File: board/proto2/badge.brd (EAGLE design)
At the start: 136.5 x 119 mm, 66 parts, among them IC1 TLV62569, J1 5051101092, J2 M05X2X1.27

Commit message: layout in process
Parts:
- added OLED1: CFAF128128B, badge:CFAF128128B
- moved C28 615.5 mm to (41.9, 92.2), turned to 305 degrees
- moved J2 590.4 mm to (43.1, 93.9), turned to 35 degrees
- moved C25 583.9 mm to (50.3, 68.8), turned to 90 degrees
- moved C24 582.9 mm to (43.2, 73.4)
- moved SD1 550.9 mm to (31.5, 69.6), turned to 35 degrees
- moved S7 548.5 mm to (90.8, 80.0), turned to 90 degrees
- moved C22 531.7 mm to (88.4, 64.9), turned to 68 degrees
- moved C20 526.9 mm to (87.9, 65.1), turned to 68 degrees
- moved C21 525.4 mm to (88.1, 65.0), turned to 68 degrees
- moved C18 519.3 mm to (88.4, 62.1), turned to 68 degrees
- moved C16 514.5 mm to (87.4, 62.5), turned to 68 degrees
- moved C17 513.1 mm to (87.9, 62.3), turned to 68 degrees
- moved C15 509.7 mm to (87.0, 62.7), turned to 68 degrees
- moved C14 502.7 mm to (87.4, 60.4), turned to 68 degrees
- moved C11 484.6 mm to (98.8, 52.8), turned to 68 degrees
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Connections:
- net N$10 renamed VIN
- net N$12 renamed FB
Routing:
- added copper zone on layer 1, net VBAT
- added copper zone on layer 1, net VIN

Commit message: lots of routing going on
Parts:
- removed C21, C22: .1u, rcl:C0402K
- moved C26 607.3 mm to (94.5, 76.2), turned to 270 degrees
- moved C27 593.5 mm to (22.6, 77.7)
- moved JP1 558.8 mm to (22.6, 71.6)
- moved C23 543.3 mm to (107.7, 51.3), turned to 90 degrees
- moved C19 538.8 mm to (104.6, 51.3), turned to 90 degrees
- moved J2 80.9 mm to (120.8, 71.2), turned to 332 degrees
- moved C28 79.9 mm to (119.1, 71.6), turned to 242 degrees
- moved C2 73.5 mm to (106.7, 55.9), turned to 270 degrees
- moved C1 73.2 mm to (109.7, 55.9), turned to 270 degrees
- moved R1 72.2 mm to (109.7, 61.0)
- moved R2 70.7 mm to (106.7, 61.0)
- moved R5 70.2 mm to (115.6, 63.5), turned to 0 degrees
- moved C5 68.5 mm to (116.1, 61.7)
- moved R3 67.7 mm to (108.2, 61.0)
- moved C3 66.2 mm to (108.2, 55.9), turned to 270 degrees
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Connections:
- net N$14 renamed SW
- net N$21 renamed P0.19
- net N$26 renamed SWDIO
- net N$31 renamed SWCLK
- net N$32 renamed P0.18
- net N$33 renamed !RESET
- net +3V3: no longer C21.1, C22.1
- net GND: no longer C21.2, C22.2
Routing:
- net GND: track 0.00 -> 74.8 mm, vias 0 -> 64
- net ANT: track 405.1 -> 470.2 mm, vias 0 -> 4
- net N$29: track 0.00 -> 50.4 mm, vias 0 -> 2
- net N$5: track 0.00 -> 37.1 mm, vias 0 -> 2
- net N$17: track 0.00 -> 30.8 mm, vias 0 -> 2
- net +3V3: track 0.00 -> 26.1 mm, vias 0 -> 2
- net N$28: track 0.00 -> 20.2 mm, vias 0 -> 2
- net N$27: track 0.00 -> 19.8 mm, vias 0 -> 2
- net P0.18: track 0.00 -> 18.3 mm, vias 0 -> 2
- net N$18: track 0.00 -> 14.6 mm, vias 0 -> 2
- net N$24: track 0.00 -> 14.0 mm, vias 0 -> 2
- net N$22: track 0.00 -> 13.4 mm, vias 0 -> 2
- net N$25: track 0.00 -> 13.0 mm, vias 0 -> 2
- net N$19: track 0.00 -> 12.9 mm, vias 0 -> 2
- net N$20: track 0.00 -> 12.8 mm, vias 0 -> 2
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- added copper zone on layer 1, net +3V3
- added copper zone on layer 1, net GND
- added copper zone on layer 16, net GND
- added copper zone on layer 1, net SW

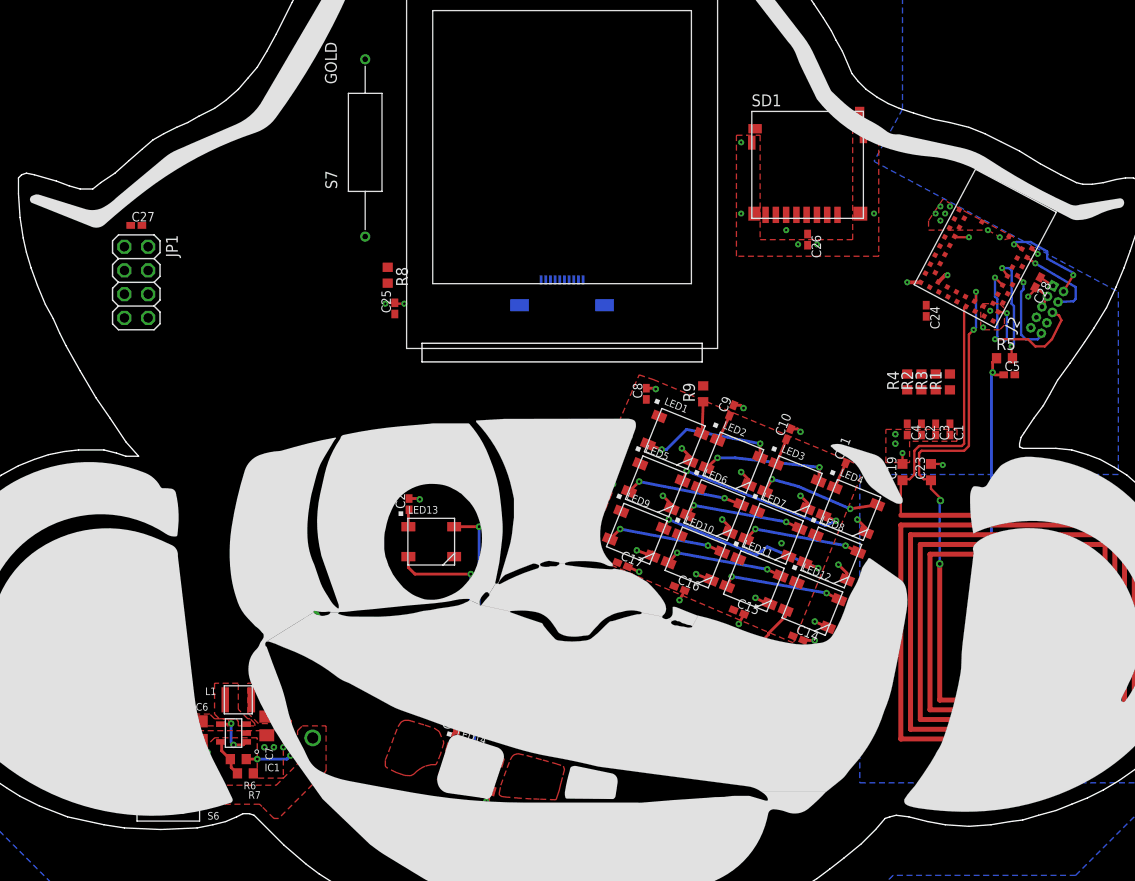
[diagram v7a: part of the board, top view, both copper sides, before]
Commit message: routing almost done.  I hate 2-layer PCBs
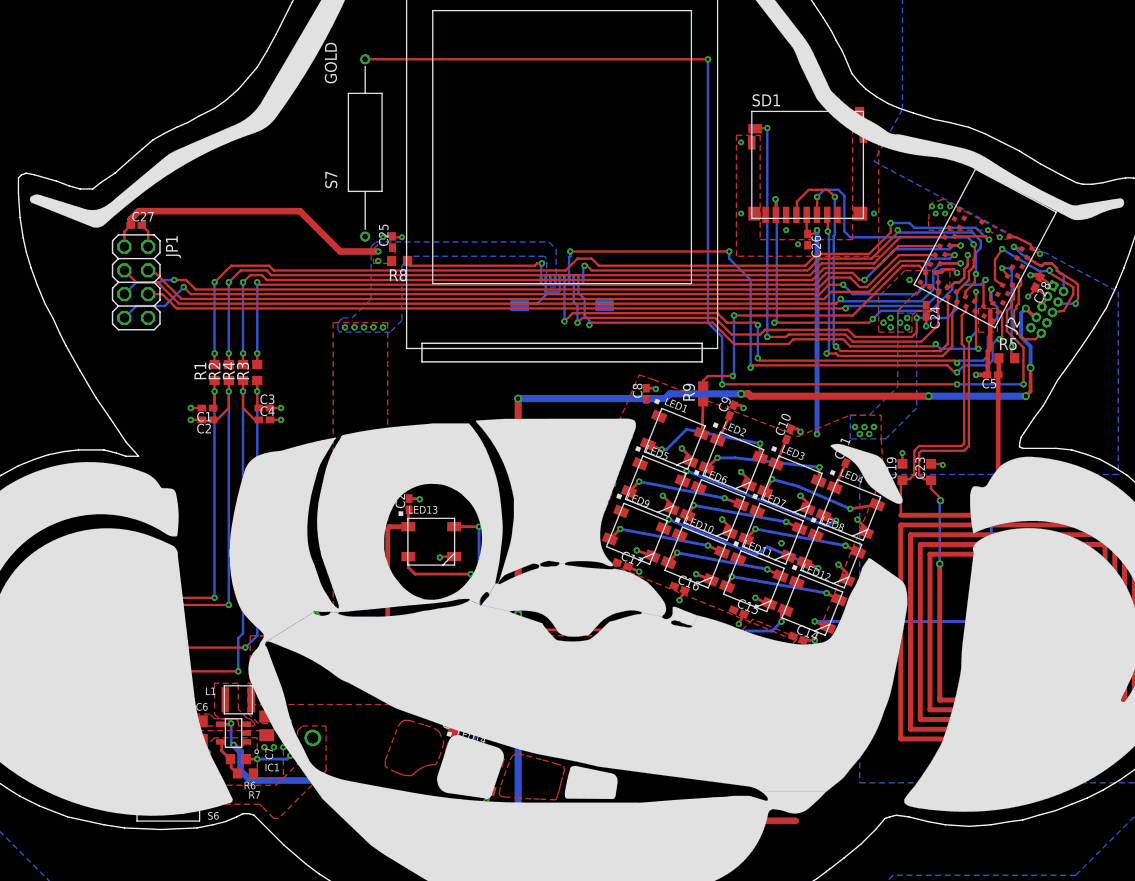
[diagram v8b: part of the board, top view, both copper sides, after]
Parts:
- moved C1 79.5 mm to (30.2, 58.2), turned to 180 degrees
- moved R1 78.7 mm to (31.0, 62.0)
- moved C2 76.5 mm to (30.2, 56.9), turned to 180 degrees
- moved R2 74.2 mm to (32.5, 62.0)
- moved R3 72.7 mm to (35.6, 62.0)
- moved C3 71.9 mm to (36.3, 58.2), turned to 0 degrees
- moved R4 71.1 mm to (34.0, 62.0)
- moved C4 68.8 mm to (36.3, 56.9), turned to 0 degrees
- moved C25 7.12 mm to (50.0, 75.9)
- moved R8 1.98 mm to (50.8, 73.9), turned to 180 degrees
- moved C5 1.78 mm to (114.3, 61.7), turned to 180 degrees
- moved R5 0.25 mm to (115.8, 63.5)
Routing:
- net VBAT: track 5.00 -> 181.6 mm, vias 2 -> 11
- net P0.19: track 0.00 -> 116.2 mm, vias 0 -> 4
- net N$6: track 1.57 -> 100.6 mm, vias 1 -> 4
- net P0.31: track 0.00 -> 96.4 mm, vias 0 -> 2
- net P0.29: track 0.00 -> 95.5 mm, vias 0 -> 3
- net P0.01: track 0.00 -> 93.1 mm, vias 0 -> 2
- net P0.30: track 0.00 -> 90.2 mm, vias 0 -> 1
- net N$7: track 0.00 -> 87.9 mm, vias 0 -> 2
- net N$8: track 0.00 -> 87.7 mm, vias 0 -> 4
- net P0.00: track 0.00 -> 86.8 mm
- net +3V3: track 26.1 -> 112.1 mm, vias 2 -> 20
- net N$9: track 0.00 -> 85.5 mm, vias 0 -> 2
- net P0.14: track 0.00 -> 64.2 mm, vias 0 -> 5
- net P0.13: track 4.10 -> 66.5 mm, vias 1 -> 5
- net P0.12: track 0.00 -> 57.3 mm, vias 0 -> 3
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- added copper zone on layer 16, net +3V3
